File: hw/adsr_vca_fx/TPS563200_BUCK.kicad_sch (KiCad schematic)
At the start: 13 parts, among them U8 TPS563200

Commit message: first draft layout
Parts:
- removed TP9: TestPoint, TestPoint:TestPoint_Pad_D1.0mm, symbol Connector:TestPoint
- renumbered C18 to C16, C19 to C17, C20 to C18, C21 to C19, C22 to C20, R24 to R21, R25 to R22, R26 to R23, TP10 to TP8, U8 to U6

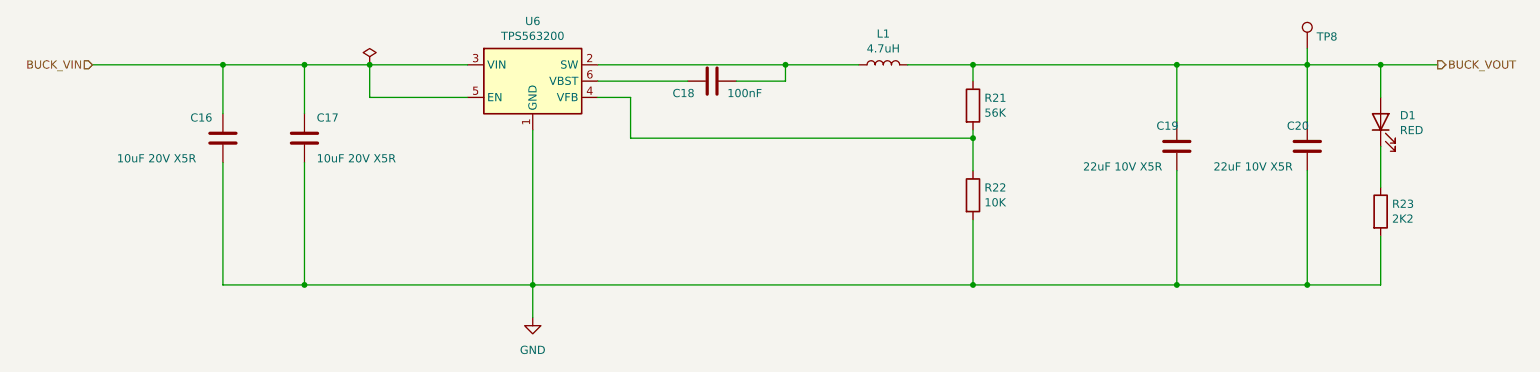
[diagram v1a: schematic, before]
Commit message: updated layout
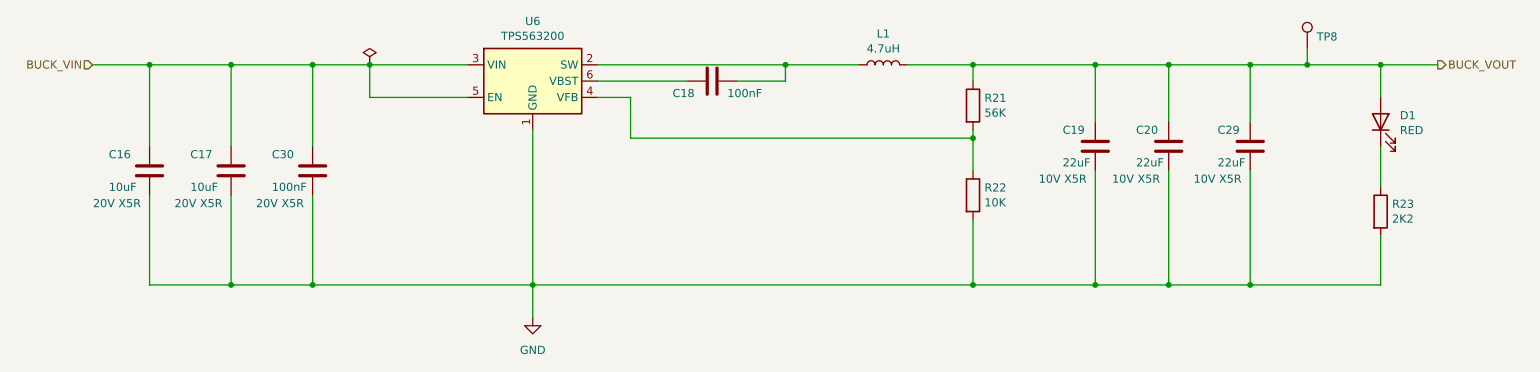
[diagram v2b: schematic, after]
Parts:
- added C29: 22uF, Resistor_SMD:R_1206_3216Metric_Pad1.30x1.75mm_HandSolder, symbol Device:C
- added C30: 100nF, Resistor_SMD:R_1206_3216Metric_Pad1.30x1.75mm_HandSolder, symbol Device:C
- C16, C17: value 10uF 20V X5R -> 10uF; Addtional (none) -> 20V X5R
- C19, C20: value 22uF 10V X5R -> 22uF; Additional (none) -> 10V X5R
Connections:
- net BUCK_VIN: now also C30.1
- net BUCK_VOUT: now also C29.1
- net GND: now also C29.2, C30.2
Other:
- moved on the sheet: C16, C19

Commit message: completed layout
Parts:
- removed TP8: TestPoint, TestPoint:TestPoint_Pad_D1.0mm, symbol Connector:TestPoint
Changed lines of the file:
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@@
   (junction (at 237.49 81.28) (diameter 0) (color 0 0 0 0)
   )
-  (junction (at 226.06 81.28) (diameter 0) (color 0 0 0 0)
-  )
   (junction (at 45.72 81.28) (diameter 0) (color 0 0 0 0)
   )
@@
     (stroke (width 0) (type default))
   )
-  (wire (pts (xy 226.06 81.28) (xy 226.06 78.74))
-    (stroke (width 0) (type default))
-  )
   (wire (pts (xy 173.99 105.41) (xy 173.99 115.57))
     (stroke (width 0) (type default))
@@
     (stroke (width 0) (type default))
   )
-  (wire (pts (xy 217.17 81.28) (xy 226.06 81.28))
+  (wire (pts (xy 217.17 81.28) (xy 237.49 81.28))
     (stroke (width 0) (type default))
   )
@@
   )
   (wire (pts (xy 173.99 92.71) (xy 120.65 92.71))
-    (stroke (width 0) (type default))
-  )
-  (wire (pts (xy 226.06 81.28) (xy 237.49 81.28))
     (stroke (width 0) (type default))
   )
@@
         )
       )
-    )
-  )
-  (symbol (lib_id "Connector:TestPoint") (at 226.06 78.74 0) (unit 1)
-    (in_bom yes) (on_board yes) (dnp no)
-    (property "Reference" "TP8" (at 227.5332 76.9112 0)
-      (effects (font (size 1.27 1.27)) (justify left))
-    )
-    (property "Value" "TestPoint" (at 227.5332 78.0542 0)
-      (effects (font (size 1.27 1.27)) (justify left) hide)
-    )
-    (property "Footprint" "TestPoint:TestPoint_Pad_D1.0mm" (at 231.14 78.74 0)
-      (effects (font (size 1.27 1.27)) hide)
-    )
-    (property "Datasheet" "~" (at 231.14 78.74 0)
-      (effects (font (size 1.27 1.27)) hide)
-    )
-    (property "LcscNo" "~" (at 226.06 78.74 0)
-      (effects (font (size 1.27 1.27)) hide)
-    )
-    (property "Type" "~" (at 226.06 78.74 0)
-      (effects (font (size 1.27 1.27)) hide)
-    )
-    (pin "1")
-    (instances
-      (project "adsr_vca_fx"
-        (path "/2c7cc946-dcca-4ffb-b6a0-bf0c9ddb491b/d2509004-b5c4-4b3c-af62-d7c90bd19790/cfda1149-d0fd-45bd-b9f5-d59eb44c2b04"
-          (reference "TP8") (unit 1)
-        )
-      )
